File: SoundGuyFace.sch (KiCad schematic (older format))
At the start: 74 parts, among them J1 NRJ6HF-1, J2 NCJ6FA-H-0, J3 UJ2-MIBH-4-MSMT-TR, SW1 SW_Push_Open, SW2 SW_Push_Open, U1 PCM2912A, U2 INA333, U3 TPS61041DBV, Y1 CSTNR6M00GH5L000R0

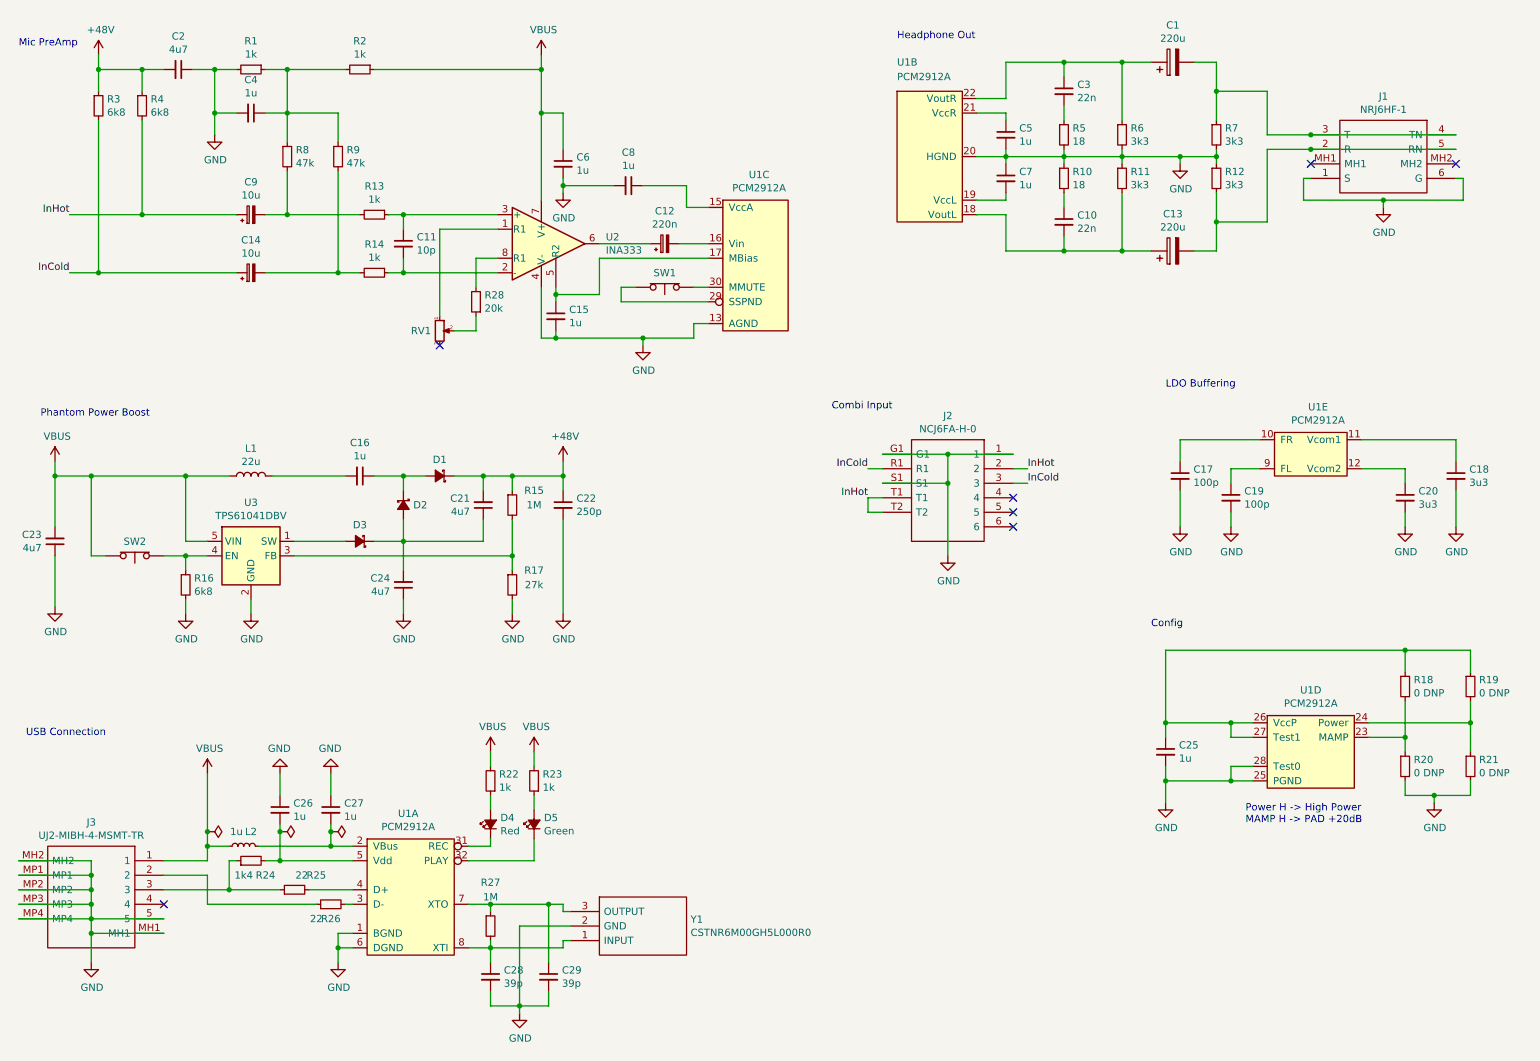
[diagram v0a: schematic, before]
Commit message: Small schematic changes and first PCB layout done
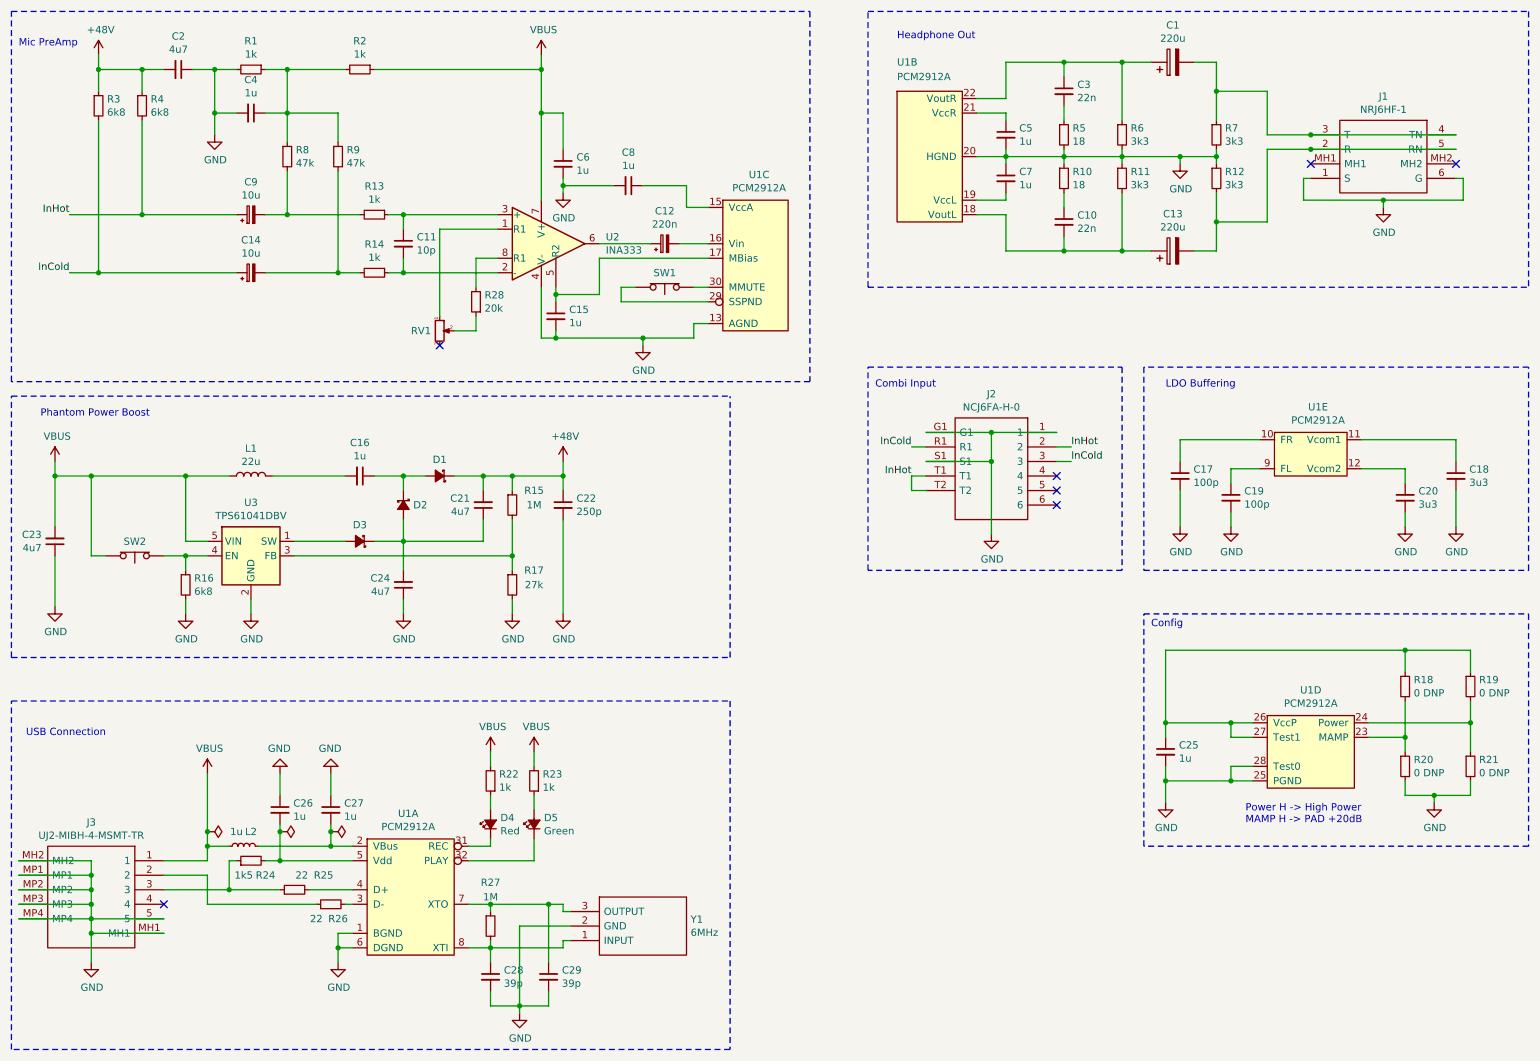
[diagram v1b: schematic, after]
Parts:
- R24: value 1k4 -> 1k5
- SW1, SW2: footprint Connector_PinHeader_2.00mm:PinHeader_1x02_P2.00mm_Vertical -> Connector_PinHeader_2.54mm:PinHeader_1x02_P2.54mm_Vertical
- Y1: value CSTNR6M00GH5L000R0 -> 6MHz
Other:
- moved on the sheet: J2
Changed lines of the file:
@@
 L SamacSys_Parts:NCJ6FA-H-0 J2
 U 1 1 5EC04E0E
-P 7550 3600
-F 0 "J2" H 8000 3865 50  0000 C CNN
-F 1 "NCJ6FA-H-0" H 8000 3774 50  0000 C CNN
-F 2 "SamacSys_Parts:NCJ6FAH0" H 8300 3700 50  0001 L CNN
-F 3 "http://www.neutrik.us/en-us/plugs-jacks/jacks/combo-a-series/ncj6fa-h-0" H 8300 3600 50  0001 L CNN
-F 4 "Socket; Jack 6,35mm + XLR; female; angled 90; THT; 3A" H 8300 3500 50  0001 L CNN "Description"
-F 5 "25" H 8300 3400 50  0001 L CNN "Height"
-F 6 "568-NCJ6FA-H-0" H 8300 3300 50  0001 L CNN "Mouser Part Number"
-F 7 "https://www.mouser.co.uk/ProductDetail/Neutrik/NCJ6FA-H-0?qs=aEaV1LakhLaCrLXco%252BtEjw%3D%3D" H 8300 3200 50  0001 L CNN "Mouser Price/Stock"
-F 8 "Neutrik" H 8300 3100 50  0001 L CNN "Manufacturer_Name"
-F 9 "NCJ6FA-H-0" H 8300 3000 50  0001 L CNN "Manufacturer_Part_Number"
-F 10 "Neutrik" H 7550 3600 50  0001 C CNN "Manufacturer"
-F 11 "NCJ6FA-H-0" H 7550 3600 50  0001 C CNN "Manufacturer Part ID"
-F 12 "568-NCJ6FA-H-0" H 7550 3600 50  0001 C CNN "Mouser ID"
-	1    7550 3600
+P 7850 3450
+F 0 "J2" H 8300 3715 50  0000 C CNN
+F 1 "NCJ6FA-H-0" H 8300 3624 50  0000 C CNN
+F 2 "SamacSys_Parts:NCJ6FAH0" H 8600 3550 50  0001 L CNN
+F 3 "http://www.neutrik.us/en-us/plugs-jacks/jacks/combo-a-series/ncj6fa-h-0" H 8600 3450 50  0001 L CNN
+F 4 "Socket; Jack 6,35mm + XLR; female; angled 90; THT; 3A" H 8600 3350 50  0001 L CNN "Description"
+F 5 "25" H 8600 3250 50  0001 L CNN "Height"
+F 6 "568-NCJ6FA-H-0" H 8600 3150 50  0001 L CNN "Mouser Part Number"
+F 7 "https://www.mouser.co.uk/ProductDetail/Neutrik/NCJ6FA-H-0?qs=aEaV1LakhLaCrLXco%252BtEjw%3D%3D" H 8600 3050 50  0001 L CNN "Mouser Price/Stock"
+F 8 "Neutrik" H 8600 2950 50  0001 L CNN "Manufacturer_Name"
+F 9 "NCJ6FA-H-0" H 8600 2850 50  0001 L CNN "Manufacturer_Part_Number"
+F 10 "Neutrik" H 7850 3450 50  0001 C CNN "Manufacturer"
+F 11 "NCJ6FA-H-0" H 7850 3450 50  0001 C CNN "Manufacturer Part ID"
+F 12 "568-NCJ6FA-H-0" H 7850 3450 50  0001 C CNN "Mouser ID"
+	1    7850 3450
 	-1   0    0    -1
 $EndComp
@@
 Wire Wire Line
 	4850 2450 4950 2450
-NoConn ~ 7550 3900
-NoConn ~ 7550 4000
-NoConn ~ 7550 4100
+NoConn ~ 7850 3750
+NoConn ~ 7850 3850
+NoConn ~ 7850 3950
 $Comp
 L power:+48V #PWR0114
@@
 InCold
 Wire Wire Line
-	6650 3900 6550 3900
-Wire Wire Line
-	6550 3900 6550 4000
-Wire Wire Line
-	6550 4000 6650 4000
-Wire Wire Line
-	6650 3700 6550 3700
-Wire Wire Line
-	7550 3700 7650 3700
-Wire Wire Line
-	7550 3800 7650 3800
+	6950 3750 6850 3750
+Wire Wire Line
+	6850 3750 6850 3850
+Wire Wire Line
+	6850 3850 6950 3850
+Wire Wire Line
+	6950 3550 6850 3550
+Wire Wire Line
+	7850 3550 7950 3550
+Wire Wire Line
+	7850 3650 7950 3650
 $Comp
 L power:GND #PWR0115
 U 1 1 5EDB66FC
-P 7100 4300
-F 0 "#PWR0115" H 7100 4050 50  0001 C CNN
-F 1 "GND" H 7105 4127 50  0000 C CNN
-F 2 "" H 7100 4300 50  0001 C CNN
-F 3 "" H 7100 4300 50  0001 C CNN
-	1    7100 4300
-	1    0    0    -1
-$EndComp
-Wire Wire Line
-	7550 3600 7100 3600
-Wire Wire Line
-	7100 3600 7100 3800
-Wire Wire Line
-	6650 3800 7100 3800
-Connection ~ 7100 3800
-Wire Wire Line
-	7100 3800 7100 4300
-Wire Wire Line
-	6650 3600 7100 3600
-Connection ~ 7100 3600
-Text Label 6550 3900 2    50   ~ 0
+P 7400 4150
+F 0 "#PWR0115" H 7400 3900 50  0001 C CNN
+F 1 "GND" H 7405 3977 50  0000 C CNN
+F 2 "" H 7400 4150 50  0001 C CNN
+F 3 "" H 7400 4150 50  0001 C CNN
+	1    7400 4150
+	1    0    0    -1
+$EndComp
+Wire Wire Line
+	7850 3450 7400 3450
+Wire Wire Line
+	7400 3450 7400 3650
+Wire Wire Line
+	6950 3650 7400 3650
+Connection ~ 7400 3650
+Wire Wire Line
+	7400 3650 7400 4150
+Wire Wire Line
+	6950 3450 7400 3450
+Connection ~ 7400 3450
+Text Label 6850 3750 2    50   ~ 0
 InHot
-Text Label 7650 3700 0    50   ~ 0
+Text Label 7950 3550 0    50   ~ 0
 InHot
-Text Label 6550 3700 2    50   ~ 0
+Text Label 6850 3550 2    50   ~ 0
 InCold
-Text Label 7650 3800 0    50   ~ 0
+Text Label 7950 3650 0    50   ~ 0
 InCold
 $Comp
@@
 U 1 1 5EE33BEE
 P 2600 6600
-F 0 "R25" V 2700 6450 50  0000 C CNN
+F 0 "R25" V 2700 6400 50  0000 C CNN
 F 1 "22" V 2700 6550 50  0000 C CNN
 F 2 "Resistor_SMD:R_0402_1005Metric" H 2600 6600 50  0001 C CNN
@@
 P 2300 6400
 F 0 "R24" V 2200 6300 50  0000 C CNN
-F 1 "1k4" V 2200 6450 50  0000 C CNN
+F 1 "1k5" V 2200 6450 50  0000 C CNN
 F 2 "Resistor_SMD:R_0402_1005Metric" H 2300 6400 50  0001 C CNN
 F 3 "https://www.mouser.de/datasheet/2/447/PYu-RC_Group_51_RoHS_L_10-1664068.pdf" H 2300 6400 50  0001 C CNN
@@
 U 1 1 5EE34876
 P 2850 6700
-F 0 "R26" V 2750 6700 50  0000 C CNN
+F 0 "R26" V 2750 6650 50  0000 C CNN
 F 1 "22" V 2750 6800 50  0000 C CNN
 F 2 "Resistor_SMD:R_0402_1005Metric" H 2850 6700 50  0001 C CNN
@@
 P 4500 6750
 F 0 "Y1" H 5328 6696 50  0000 L CNN
-F 1 "CSTNR6M00GH5L000R0" H 5328 6605 50  0000 L CNN
+F 1 "6MHz" H 5328 6605 50  0000 L CNN
 F 2 "SamacSys_Parts:CSTNR6M00GH5L000R0" H 5350 6850 50  0001 L CNN
 F 3 "https://componentsearchengine.com/Datasheets/1/CSTNR6M00GH5L000R0.pdf" H 5350 6750 50  0001 L CNN
@@
 Text Notes 750  5550 0    50   ~ 0
 USB Connection
-Text Notes 6300 3300 0    50   ~ 0
+Text Notes 6600 3150 0    50   ~ 0
 Combi Input
 $Comp
@@
 F 0 "SW2" H 1500 4201 50  0000 C CNN
 F 1 "SW_Push_Open" H 1500 4201 50  0001 C CNN
-F 2 "Connector_PinHeader_2.00mm:PinHeader_1x02_P2.00mm_Vertical" H 1500 4500 50  0001 C CNN
+F 2 "Connector_PinHeader_2.54mm:PinHeader_1x02_P2.54mm_Vertical" H 1500 4500 50  0001 C CNN
 F 3 "~" H 1500 4500 50  0001 C CNN
 	1    1500 4300
@@
 F 0 "SW1" H 5150 2351 50  0000 C CNN
 F 1 "SW_Push_Open" H 5150 2351 50  0001 C CNN
-F 2 "Connector_PinHeader_2.00mm:PinHeader_1x02_P2.00mm_Vertical" H 5150 2650 50  0001 C CNN
+F 2 "Connector_PinHeader_2.54mm:PinHeader_1x02_P2.54mm_Vertical" H 5150 2650 50  0001 C CNN
 F 3 "~" H 5150 2650 50  0001 C CNN
 	1    5150 2450
@@
 Wire Wire Line
 	3600 2050 3600 2650
+Wire Notes Line
+	650  5000 650  3200
+Wire Notes Line
+	650  5300 5600 5300
+Wire Notes Line
+	5600 5300 5600 7700
+Wire Notes Line
+	5600 7700 650  7700
+Wire Notes Line
+	650  7700 650  5300
+Wire Notes Line
+	8450 4700 11100 4700
+Wire Notes Line
+	11100 4700 11100 6300
+Wire Notes Line
+	11100 6300 8450 6300
+Wire Notes Line
+	8450 6300 8450 4700
+Wire Notes Line
+	8450 4400 11100 4400
+Wire Notes Line
+	11100 4400 11100 3000
+Wire Notes Line
+	11100 3000 8450 3000
+Wire Notes Line
+	8450 3000 8450 4400
+Wire Notes Line
+	11100 550  11100 2450
+Wire Notes Line
+	6550 2450 6550 550
+Wire Notes Line
+	650  550  6150 550
+Wire Notes Line
+	6150 550  6150 3100
+Wire Notes Line
+	6150 3100 650  3100
+Wire Notes Line
+	650  3100 650  550
+Wire Notes Line
+	6550 3000 8300 3000
+Wire Notes Line
+	8300 3000 8300 4400
+Wire Notes Line
+	8300 4400 6550 4400
+Wire Notes Line
+	6550 4400 6550 3000
+Wire Notes Line
+	6550 2450 11100 2450
+Wire Notes Line
+	6550 550  11100 550
+Wire Notes Line
+	5600 5000 5600 3200
+Wire Notes Line
+	650  3200 5600 3200
+Wire Notes Line
+	650  5000 5600 5000
 $EndSCHEMATC

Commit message: Version to dispatch
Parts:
- J1: Mouser ID (none) -> 550-20384
- J3: Mouser ID (none) -> 490-UJ2-MIBH-4-MSMT
- U1: Manufacturer (none) -> Texas Instruments; Manufacturer Part ID (none) -> PCM2912APJTR; Mouser ID (none) -> 595-PCM2912APJTR
- Y1: Mouser ID (none) -> 81-CSTNR6M00GH5L000R
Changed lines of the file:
@@
 F 2 "Package_QFP:TQFP-32_7x7mm_P0.8mm" H 3450 5250 50  0001 C CNN
 F 3 "http://www.ti.com/general/docs/suppproductinfo.tsp?distId=26&gotoUrl=http%3A%2F%2Fwww.ti.com%2Flit%2Fgpn%2Fpcm2912a" H 3450 5250 50  0001 C CNN
+F 4 "Texas Instruments" H 3100 6250 50  0001 C CNN "Manufacturer"
+F 5 "PCM2912APJTR" H 3100 6250 50  0001 C CNN "Manufacturer Part ID"
+F 6 "595-PCM2912APJTR" H 3100 6250 50  0001 C CNN "Mouser ID"
 	1    3100 6250
 	1    0    0    -1
@@
 F 8 "Neutrik" H 11450 900 50  0001 L CNN "Manufacturer_Name"
 F 9 "NRJ6HF-1" H 11450 800 50  0001 L CNN "Manufacturer_Part_Number"
+F 10 "550-20384" H 10600 1400 50  0001 C CNN "Mouser ID"
 	1    10600 1400
 	-1   0    0    -1
@@
 F 8 "CUI Devices" H 2550 5900 50  0001 L CNN "Manufacturer_Name"
 F 9 "UJ2-MIBH-4-MSMT-TR" H 2550 5800 50  0001 L CNN "Manufacturer_Part_Number"
+F 10 "490-UJ2-MIBH-4-MSMT" H 1700 6400 50  0001 C CNN "Mouser ID"
 	1    1700 6400
 	-1   0    0    -1
@@
 F 8 "Murata Electronics" H 5350 6250 50  0001 L CNN "Manufacturer_Name"
 F 9 "CSTNR6M00GH5L000R0" H 5350 6150 50  0001 L CNN "Manufacturer_Part_Number"
+F 10 "81-CSTNR6M00GH5L000R" H 4500 6750 50  0001 C CNN "Mouser ID"
 	1    4500 6750
 	1    0    0    -1
